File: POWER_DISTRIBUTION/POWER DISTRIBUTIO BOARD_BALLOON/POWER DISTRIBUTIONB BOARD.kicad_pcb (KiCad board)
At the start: 2 copper layers, 75 x 55 mm, 99 parts, among them IC3 TPS1HB08BQPWPRQ1, IC4 TPS1HB08BQPWPRQ1, IC8 INA232AIDDFR, IC9 TCAN1044VDDFR, J10 Conn_01x02, J11 Conn_01x02, J28 Conn_01x06, J29 Conn_01x02, J30 Conn_01x02, J31 Conn_01x02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

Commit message: POWER BOARD LAYOUT COMPLETE
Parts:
- removed D7, D9: BAS21, Package_TO_SOT_SMD:SOT-23
- removed F1: 0154005.DRL, SamacSys_Parts:0154005DRL
- removed Q1, Q2: IPD047N03LF2SATMA1, SamacSys_Parts:IPD047N03LF2SATMA1
- removed R48, R50: 4.7k, Resistor_SMD:R_0603_1608Metric
- added F2: 0154005.DRL, SamacSys_Parts:0154005DRL, F.Cu at (184.2, 116.0)
- added Q3: RSS070N05HZGTB, SamacSys_Parts:SOIC127P600X175-8N, F.Cu at (204.4, 129.2)
- added Q4: RSS070N05HZGTB, SamacSys_Parts:SOIC127P600X175-8N, F.Cu at (204.4, 135.9)
- D5, D6, PS3, R42, R43, R44, R45, TP28, TP29: moved to B.Cu
- moved R9 150.1 mm to (193.0, 84.8), turned to 90 degrees
- moved R8 148.3 mm to (191.2, 84.8), turned to 90 degrees
- moved R16 146.9 mm to (193.8, 96.4), turned to 90 degrees
- moved J34 145.4 mm to (214.0, 140.0)
- moved R15 145.0 mm to (191.8, 96.4), turned to 90 degrees
- moved R5 141.4 mm to (180.1, 81.5)
- moved R7 141.3 mm to (180.1, 86.7)
- moved R4 141.1 mm to (180.1, 85.0)
- moved R3 141.1 mm to (180.1, 83.2)
- moved TP11 140.7 mm to (219.8, 127.6)
- moved D2 139.5 mm to (178.8, 98.7), turned to 90 degrees
- moved D1 139.4 mm to (178.6, 89.7), turned to -90 degrees
- moved R10 137.8 mm to (180.1, 103.4)
- moved R11 137.7 mm to (180.1, 105.2)
- moved R6 137.6 mm to (176.6, 93.2)
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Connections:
- C10 pad 2: 12VDC -> VBAT+
- C13 pad 2: Net-(PS3-+VIN) -> VBAT_Fused
- C15 pad 2: Net-(PS3-+VIN) -> VBAT_Fused
- C17 pad 2: Net-(PS3-+VIN) -> VBAT_Fused
- C19 pad 2: Net-(PS3-+VIN) -> VBAT_Fused
- C47 pad 2: VCC_BALANCE -> +3.3V
- C9 pad 2: 12VDC -> VBAT+
- IC3 pad 17: 12VDC -> VBAT+
- IC4 pad 17: 12VDC -> VBAT+
- IC8 pad 1: VBAT+ -> VBAT_Fused
- IC8 pad 2: VBAT+ -> VBAT_Fused
- PS3 pad 1: Net-(PS3-+VIN) -> VBAT_Fused
- R52 pad 1: VBAT+ -> VBAT_Fused
- R52 pad 2: VBAT+ -> VBAT_Fused
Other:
- board size 75 x 55 mm -> 74.5 x 55 mm
- board text added: "+"
- board text added: "PWR1"
- board text added: "PWR2"
- board text added: "PWR3"

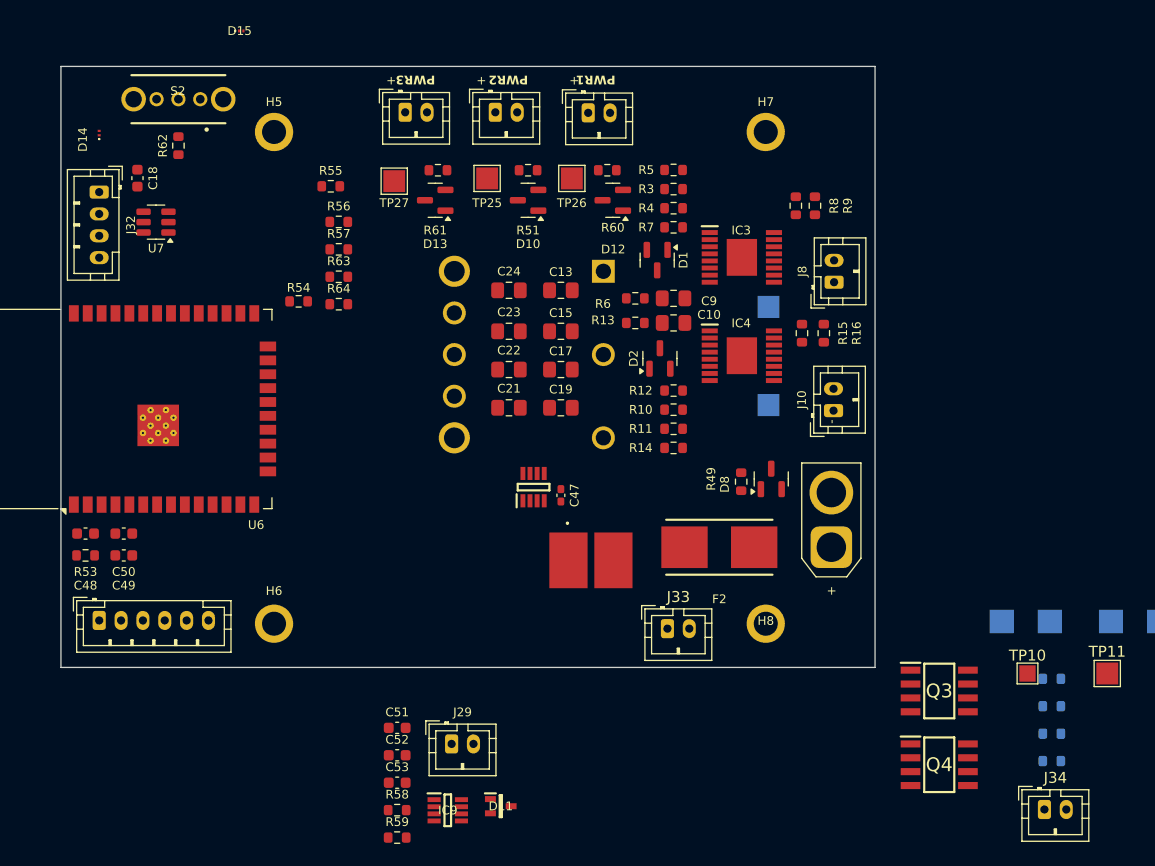
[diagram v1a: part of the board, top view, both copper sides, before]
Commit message: added some global labels
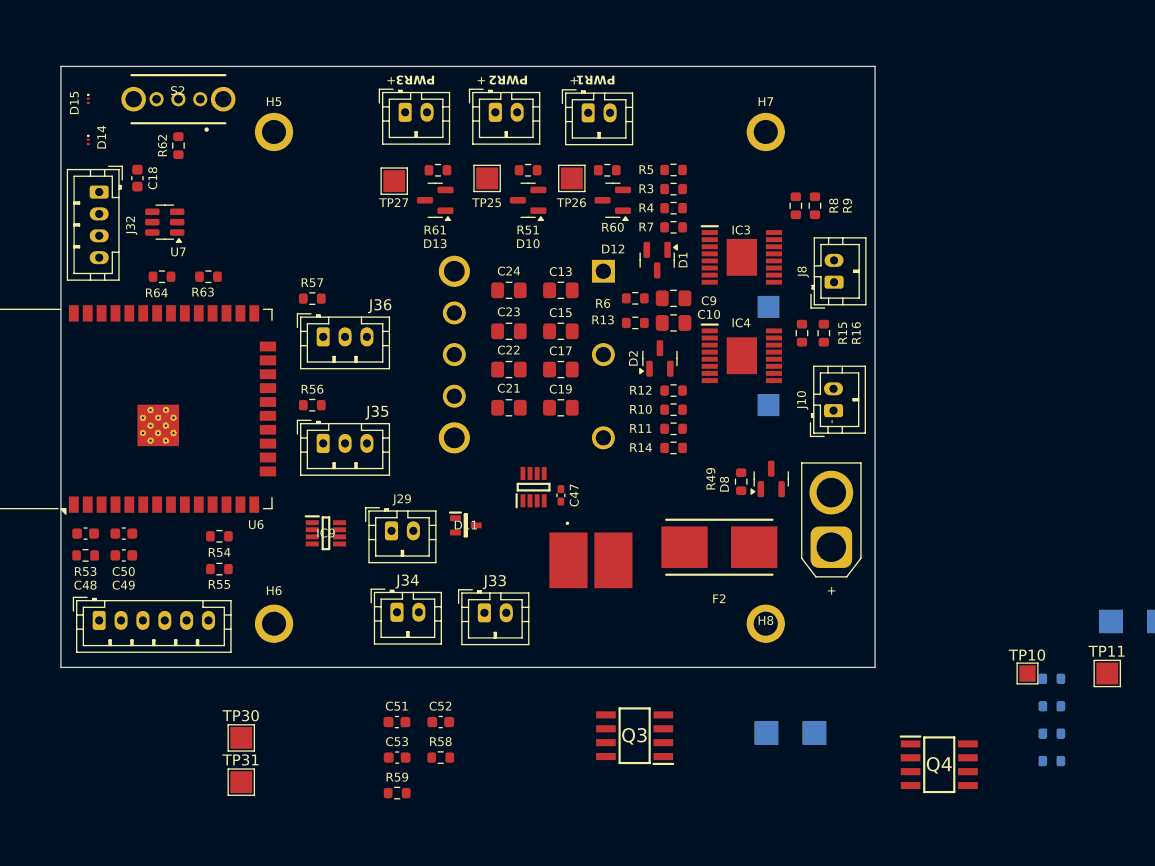
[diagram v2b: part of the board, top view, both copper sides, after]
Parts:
- added J35: Conn_01x03, Connector_JST:JST_PH_B3B-PH-K_1x03_P2.00mm_Vertical, F.Cu at (148.0, 106.5)
- added J36: Conn_01x03, Connector_JST:JST_PH_B3B-PH-K_1x03_P2.00mm_Vertical, F.Cu at (148.0, 96.8)
- added TP30: S2761-46R, TestPoint:TestPoint_Pad_2.0x2.0mm, F.Cu at (140.5, 133.4)
- added TP31: S2761-46R, TestPoint:TestPoint_Pad_2.0x2.0mm, F.Cu at (140.5, 137.5)
- moved J34 61.9 mm to (154.8, 122.0)
- moved R55 36.5 mm to (138.5, 118.0), turned to 180 degrees
- moved Q3 28.2 mm to (176.5, 133.2), turned to 180 degrees
- moved IC9 27.7 mm to (148.2, 114.7)
- moved D11 25.9 mm to (161.1, 114.0)
- moved D6 23.8 mm to (190.8, 133.0)
- moved R54 22.7 mm to (138.5, 115.0), turned to 180 degrees
- moved J29 20.3 mm to (154.2, 114.5)
- moved R56 16.9 mm to (147.0, 103.0)
- moved J33 16.8 mm to (162.8, 122.0)
- moved R64 16.4 mm to (133.2, 91.2), turned to 180 degrees
- moved D15 15.2 mm to (126.5, 75.0), turned to -90 degrees
- moved R63 11.9 mm to (137.5, 91.2), turned to 180 degrees
- moved R58 6.24 mm to (158.8, 135.2)
- moved R57 5.12 mm to (147.0, 93.2)
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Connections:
- IC9 pad 1: CAN_RX_FILT_1 -> CAN_TX
- IC9 pad 4: CAN_TX_FILT_1 -> CAN_RX

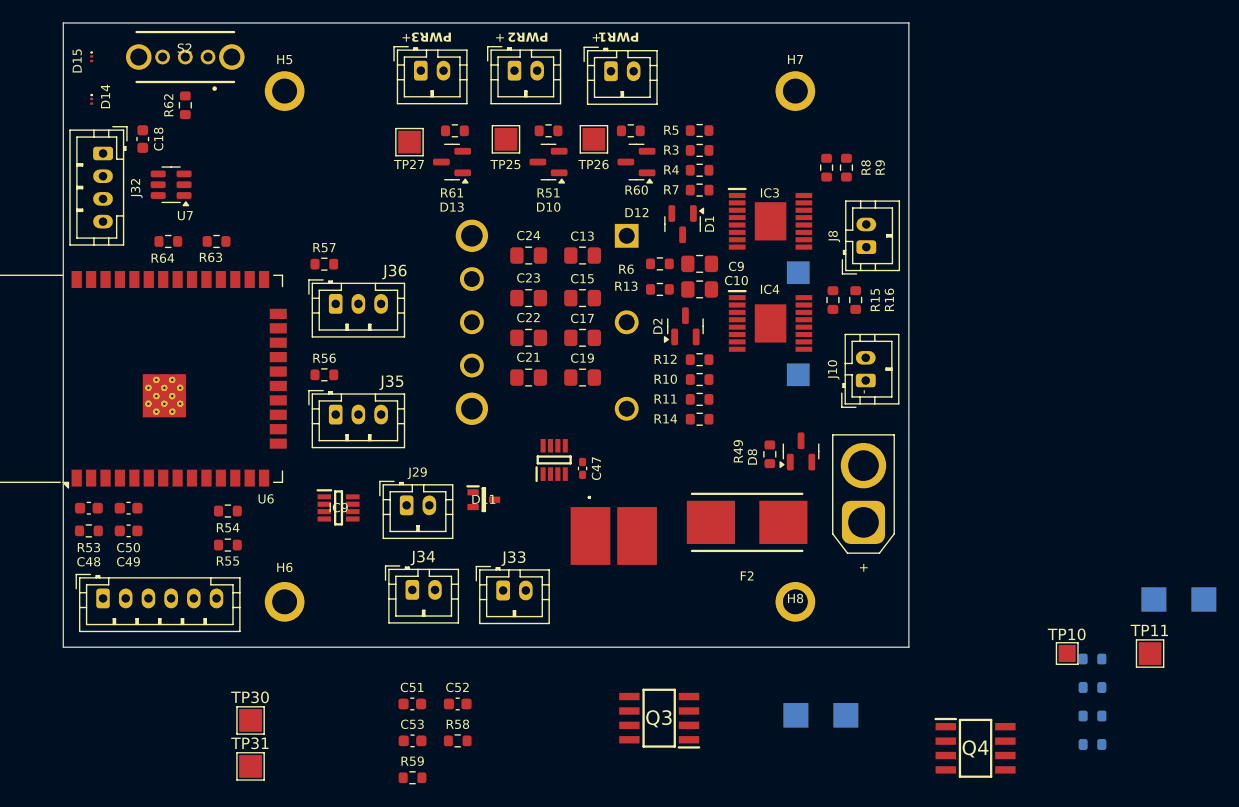
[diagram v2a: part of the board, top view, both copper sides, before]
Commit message: almost finished wiring
btw for the i2c bus idk if it was meant to be SCL instead of SDL , there is alr an SDA line but i assume so
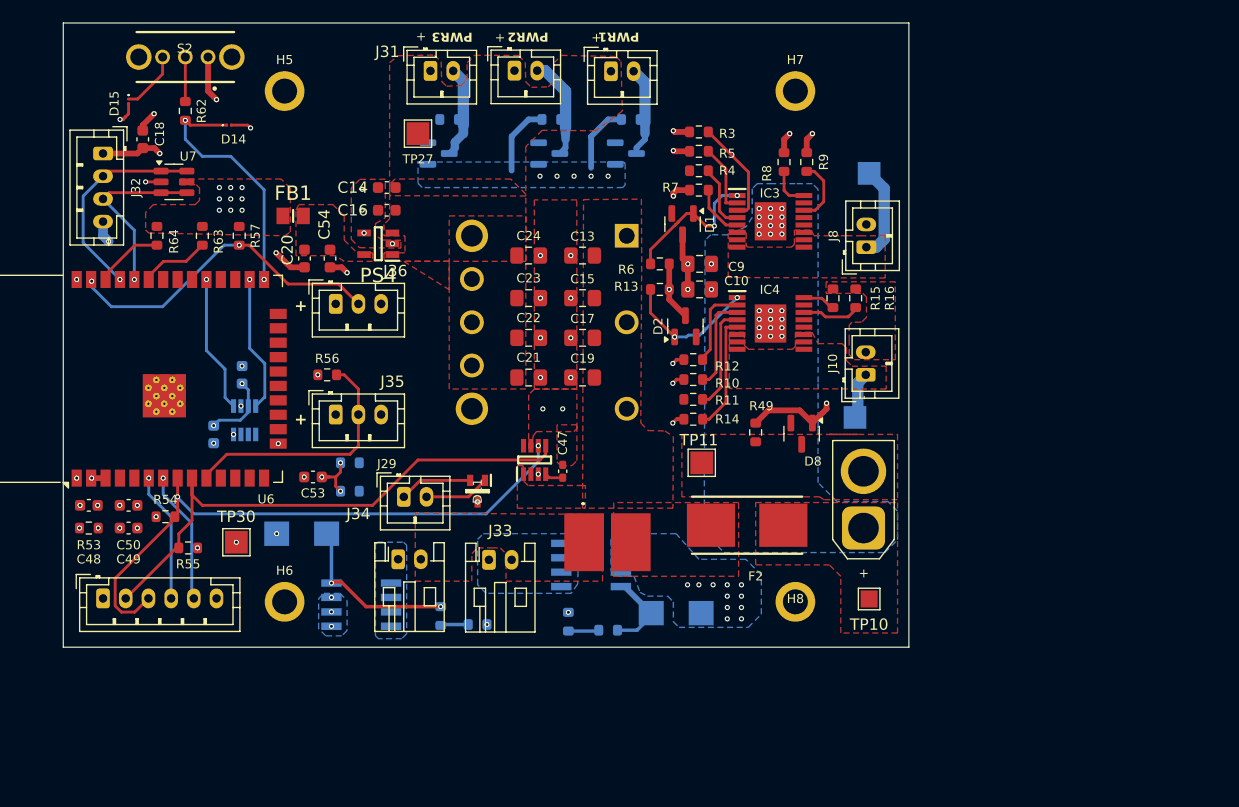
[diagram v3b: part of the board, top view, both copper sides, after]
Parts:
- removed TP25, TP26, TP31: S2761-46R, TestPoint:TestPoint_Pad_2.0x2.0mm
- added C14: 1uF, Capacitor_SMD:C_0603_1608Metric, F.Cu at (152.5, 86.5)
- added C16: 100nF, Capacitor_SMD:C_0603_1608Metric, F.Cu at (152.5, 88.5)
- added C20: 1uF, Capacitor_SMD:C_0603_1608Metric, F.Cu at (145.2, 92.8)
- added C54: 100nF, Capacitor_SMD:C_0603_1608Metric, F.Cu at (147.5, 92.8)
- added FB1: BLM21PG221SN1D, SamacSys_COMMS:BEADC2012X105N, F.Cu at (144.2, 89.0)
- added PS4: TLV75733PDBVR, SamacSys_COMMS:SOT95P280X145-5N, F.Cu at (151.8, 91.5)
- C51, C52, D10, D12, D13, IC9, R51, R58, R59, R60, R61: moved to B.Cu
- J33, J34: footprint Connector_JST:JST_PH_B2B-PH-K_1x02_P2.00mm_Vertical -> Connector_JST:JST_PH_S2B-PH-K_1x02_P2.00mm_Horizontal
- Q3, Q4: footprint SamacSys_Parts:SOIC127P600X175-8N -> SamacSys_COMMS:SOIC127P600X175-8N; moved to B.Cu
- moved R45 58.5 mm to (157.2, 124.2), turned to -90 degrees
- moved R44 54.8 mm to (160.5, 125.0)
- moved D6 48.5 mm to (145.0, 117.0)
- moved R42 46.3 mm to (168.5, 124.8), turned to -90 degrees
- moved D5 44.3 mm to (178.0, 124.0), turned to 180 degrees
- moved R43 43.0 mm to (172.0, 125.5)
- moved TP11 42.9 mm to (180.2, 110.8)
- moved Q4 37.5 mm to (170.5, 119.8), turned to 180 degrees
- moved C51 32.6 mm to (139.8, 103.0), turned to 90 degrees
- moved C52 32.0 mm to (137.2, 108.2), turned to -90 degrees
- moved R59 28.3 mm to (149.2, 110.8), turned to 180 degrees
- moved Q3 28.1 mm to (150.2, 123.2), turned to 0 degrees
- moved C53 24.8 mm to (146.0, 112.0), turned to 180 degrees
- moved R58 24.0 mm to (149.2, 113.2)
- moved TP10 18.1 mm to (195.0, 122.8), turned to 180 degrees
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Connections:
- D10 pad 3: GND -> Net-(D10-K)
- D12 pad 3: GND -> Net-(D12-K)
- D13 pad 3: GND -> Net-(D13-K)
- D8 pad 1: Net-(D8-A) -> GND
- D8 pad 3: GND -> /EXTERNAL CONNECTORS/BAS_IN
- IC8 pad 2: VBAT_Fused -> VBAT_Fused_OUT
- IC8 pad 5: I2C2_SCL -> I2C2_SDL
- J11 pad 2: Net-(D8-A) -> /EXTERNAL CONNECTORS/BAS_IN
- J30 pad 2: GND -> Net-(D12-K)
- J31 pad 2: GND -> Net-(D13-K)
- J32 pad 2: Net-(J32-Pin_2) -> PGM_RX
- J32 pad 3: Net-(J32-Pin_3) -> PGM_TX
- J33 pad 2: VBAT+ -> VBAT_Fused_OUT
- J34 pad 1: PYR_1 -> PYR_2
- J34 pad 2: VBAT+ -> VBAT_Fused_OUT
- J9 pad 2: GND -> Net-(D10-K)
- R11 pad 1: unconnected-(R11-Pad1) -> HEATER_EN
- R49 pad 1: Net-(D8-A) -> /EXTERNAL CONNECTORS/BAS_IN
- R51 pad 1: GND -> Net-(D10-K)
- R52 pad 1: VBAT_Fused -> VBAT_Fused_OUT
- R60 pad 1: GND -> Net-(D12-K)
- R61 pad 1: GND -> Net-(D13-K)
- TP11 pad 1: Net-(D8-A) -> /EXTERNAL CONNECTORS/BAS_IN
- U6 pad 11: CAM_SWITCH -> HEATER_EN
- U7 pad 4: Net-(J32-Pin_3) -> PGM_TX
- U7 pad 6: Net-(J32-Pin_2) -> PGM_RX
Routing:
- net GND: track 0.00 -> 60.8 mm, vias 0 -> 70
- net I2C2_SDA: track 0.00 -> 52.9 mm, vias 0 -> 2
- net I2C2_SDL: track 0.00 -> 48.7 mm
- net onewire2: track 0.00 -> 29.1 mm, vias 0 -> 2
- net BOOT: track 0.00 -> 22.2 mm, vias 0 -> 2
- net onewire1: track 0.00 -> 22.2 mm
- net PGM_RX: track 0.00 -> 18.7 mm, vias 0 -> 1
- net +3V3: track 0.00 -> 18.4 mm, vias 0 -> 21
- net PGM_TX: track 0.00 -> 15.9 mm, vias 0 -> 1
- net Net-(Q3-GATE): track 0.00 -> 15.1 mm, vias 0 -> 2
- net Net-(D1-A): track 0.00 -> 13.0 mm, vias 0 -> 2
- net CAN_TX: track 0.00 -> 12.1 mm, vias 0 -> 1
- net CAN_RX: track 0.00 -> 12.1 mm, vias 0 -> 1
- net Net-(D2-A): track 0.00 -> 12.0 mm, vias 0 -> 2
- net VTX_EN: track 0.00 -> 11.7 mm, vias 0 -> 1
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- added copper zone on F.Cu, net +3V3
- added copper zone on In2.Cu, net +3V3
- added copper zone on F.Cu, net +5V0
- added copper zone on F.Cu, net /EXTERNAL CONNECTORS/BAS_IN
- added copper zone on F.Cu, net 12V_BUS1
- added copper zone on F.Cu, net 12V_BUS2
- added copper zone on B.Cu, net GND
- added copper zone on F.Cu, net GND
- added copper zone on In1.Cu, net GND
- added copper zone on F.Cu, net Net-(PS4-OUT)
- added copper zone on B.Cu, net PYR_1
- added copper zone on B.Cu, net PYR_2
- added copper zone on B.Cu, net VBAT+
- added copper zone on F.Cu, net VBAT+
- added copper zone on F.Cu, net VBAT_Fused
- added copper zone on F.Cu, net VBAT_Fused_OUT
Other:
- copper layers 2 -> 4
